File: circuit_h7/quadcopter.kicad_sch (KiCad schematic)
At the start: 110 parts, among them J10 Conn_01x01_Female, J11 Conn_01x04_Male, J12 Conn_01x04_Male, J13 Conn_01x01_Female, J16 Conn_01x01_Female, J17 Conn_01x01_Female, J18 USB_C_Receptacle_USB2.0, J19 Conn_01x08_Male, J21 Conn_01x01_Female, J22 Conn_01x01_Female, J23 Conn_01x01_Female, J24 Conn_01x01_Female, J25 Conn_01x01_Female, J26 Conn_01x01_Female, J28 Conn_01x01_Female, J29 Conn_01x01_Female, J3 Conn_01x01_Female, J30 Conn_01x01_Female, J31 Conn_01x01_Female, J32 Conn_01x01_Female, J33 Conn_01x01_Female, J37 Conn_01x01_Female, J4 Conn_01x01_Female, J40 Conn_01x01_Female, J41 Conn_01x01_Female, J42 Conn_01x01_Female, J43 Conn_01x01_Female, J44 Conn_01x01_Female, J45 Conn_01x01_Female, J47 Conn_01x01_Female, J48 Conn_01x01_Female, J49 Conn_01x01_Female, J5 Conn_Coaxial, J50 Conn_01x01_Female, J6 Conn_01x06_Male, J7 Conn_01x01_Female, J8 Conn_01x01_Female, J9 Conn_01x01_Female, Q1 AO3400A, SW1 SW_DIP_x01, U1 STM32F103VDHx, U2 ICM-42605, U3 DPS310, U4 3V3, U5 EUP3458 1.2A, 30V max input, 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, U6 2450FM07D0034T, U7 W25Q80DVUXIE TR (16M), U8 SX1281, U9 5v, 500mA, Y1 16M, Y2 52Mhz, 12pF

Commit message: Refactored baro/alt module, including applying calibration and temp comp
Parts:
- removed R6: 510, Resistor_SMD:R_0402_1005Metric, symbol Device:R
- added J?: Conn_01x06_Male, Connector_JST:JST_SH_BM06B-SRSS-TB_1x06-1MP_P1.00mm_Vertical, symbol Connector:Conn_01x06_Male
- U7: footprint Anyleaf_Shared:USON-8_2.0x3.0mm_P0.5mm -> Package_SON:WSON-8-1EP_6x5mm_P1.27mm_EP3.4x4.3mm; Digikey W25Q80DVUXIETR-ND -> (none)
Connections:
- net +10V: now also J?.6 (Pin_6)
- net GND: now also J?.2 (Pin_2), J?.5 (Pin_5)
- net UART1_RX: now also J?.1 (Pin_1)
- net UART2_RX: now also J?.3 (Pin_3)
- net UART2_TX: now also J?.4 (Pin_4)
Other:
- note removed: "todo: Bigger flash, on back side?"
- moved on the sheet: J6

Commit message: refactored state into sep module; moved some code to statevolatile that were individual resources.
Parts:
- removed J?: Conn_01x06_Male, Connector_JST:JST_SH_BM06B-SRSS-TB_1x06-1MP_P1.00mm_Vertical, symbol Connector:Conn_01x06_Male
- removed U1: STM32F103VDHx, Package_BGA:LFBGA-100_10x10mm_Layout10x10_P0.8mm, symbol MCU_ST_STM32F1:STM32F103VDHx
- added J1: Conn_01x04_Male, Connector_JST:JST_SH_SM04B-SRSS-TB_1x04-1MP_P1.00mm_Horizontal, symbol Connector:Conn_01x04_Male
- added J14, J2: Conn_01x01_Female, TestPoint:TestPoint_Pad_2.0x2.0mm, symbol Connector:Conn_01x01_Female
- added U1: STM32H723VGH6, Package_BGA:TFBGA-100_8x8mm_Layout10x10_P0.8mm, symbol Anyleaf_Shared:STM32H723VGH6
- J13, J25, J26, J28, J29, J4: footprint TestPoint:TestPoint_Pad_1.5x1.5mm -> TestPoint:TestPoint_Pad_2.0x2.0mm
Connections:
- net +3V3: now also J1.4 (Pin_4), U1.B2 (VBAT), U1.D2 (VDD), U1.F4 (VDD), U1.F5 (VDD), U1.H1 (VDDA), U1.K1 (VDD); no longer U7.3 (IO2), U7.7 (IO3)
- net BATT_DIV: now also U1.C3 (PE4)
- net BOOT0: now also U1.B4 (PB8), U1.D5 (BOOT0)
- net BUZZER_PWM: now also U1.G6 (PE10)
- net CS_ELRS: now also U1.B1 (PC15-OSC32_OUT)
- net CS_FLASH: now also U1.F10 (PC6)
- net CS_IMU: now also U1.K8 (PB12)
- net CUR_DIV: now also U1.G5 (PB2)
- net ELRS_BUSY: now also U1.A1 (PC14-OSC32_IN)
- net ELRS_DIO: now also U1.A2 (PC13)
- net GND: now also J1.3 (Pin_3), U1.C2 (VSS), U1.E4 (VSS), U1.E5 (VSS), U1.E6 (VSS), U1.F7 (PDR_ON), U1.G1 (VSSA), U1.J1 (VSS)
- net IMU_INTERRUPT: now also U1.G4 (PC4)
- net M1: now also U1.D4 (PE0)
- net M2: now also U1.C4 (PE1)
- net M3: now also U1.J4 (PB0)
- net M4: now also U1.K4 (PB1)
- net MISO_1: now also U1.E3 (PE6)
- net MISO_2: now also U1.H10 (PB14)
- net MISO_3: now also U1.A6 (PB4)
- net MOSI_1: now also U1.H5 (PE7)
- net MOSI_2: now also U1.G10 (PB15)
- net MOSI_3: now also U1.C5 (PB5)
- net NRST: now also U1.E1 (NRST)
- net OSC_IN: now also U1.C1 (PH0-OSC_IN)
- net OSC_OUT: now also U1.D1 (PH1-OSC_OUT)
- net SCK_1: now also U1.D3 (PE5)
- net SCK_2: now also U1.J8 (PB13)
- net SCK_3: now also U1.A7 (PB3)
- net SCL1: now also J1.1 (Pin_1), U1.H7 (PE15)
- net SCL2: now also U1.K5 (PE9)
- net SDA1: now also J1.2 (Pin_2), U1.A4 (PB9)
- net SDA2: now also U1.J5 (PE8)
- net SWCLK: now also U1.G7 (PE14)
- net SWDIO: now also U1.K6 (PE13)
- net UART1_RX: now also U1.A5 (PB7)
- net UART1_TX: now also U1.B5 (PB6)
- net UART2_RX: now also U1.B3 (PE3)
- net UART2_TX: now also U1.A3 (PE2)
- net UART3_RX: now also U1.K7 (PB11)
- net UART3_TX: now also U1.J7 (PB10)
- net UART4_RX: now also U1.B8 (PC11)
- net UART4_TX: now also U1.C8 (PC12)
- net USB_DN: now also U1.H6 (PE11)
- net USB_DP: now also U1.J6 (PE12)
- new net QSPI2_IO2: U7.3 (IO2)
- new net QSPI2_IO3: U7.7 (IO3)
- new net UART5_RX: J14.1 (Pin_1)
- new net UART5_TX: J2.1 (Pin_1)
- no-connect marks 8 -> 11
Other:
- moved on the sheet: C10, C11, C12, C13, C16, C17, C18, C6, C9, J11, J12, J40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

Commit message: More work on routing
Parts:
- added J15: Conn_01x01_Female, TestPoint:TestPoint_Pad_2.0x2.0mm, symbol Connector:Conn_01x01_Female
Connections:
- net +3V3: now also J15.1 (Pin_1)
- net BATT_DIV: now also U1.G3 (PA4); no longer U1.C3 (PE4)
- net BUZZER_PWM: now also U1.D10 (PA10); no longer U1.G6 (PE10)
- net CS_FLASH: now also U1.B9 (PC10); no longer U1.F10 (PC6)
- net CS_IMU: now also U1.G4 (PC4); no longer U1.K8 (PB12)
- net IMU_INTERRUPT: now also U1.K8 (PB12); no longer U1.G4 (PC4)
- net M1: now also U1.F10 (PC6); no longer U1.D4 (PE0)
- net M2: now also U1.E10 (PC7); no longer U1.C4 (PE1)
- net M3: now also U1.F9 (PC8); no longer U1.J4 (PB0)
- net M4: now also U1.E9 (PC9); no longer U1.K4 (PB1)
- net MISO_1: now also U1.J3 (PA6); no longer U1.E3 (PE6)
- net MOSI_1: now also U1.K3 (PA7); no longer U1.H5 (PE7)
- net SCK_1: now also U1.H3 (PA5); no longer U1.D3 (PE5)
- net SCL1: now also U1.A8 (PA15); no longer U1.H7 (PE15)
- net SCL2: now also U1.C9 (PA9); no longer U1.K5 (PE9)
- net SDA2: now also U1.D9 (PA8); no longer U1.J5 (PE8)
- net SWCLK: now also U1.A9 (PA14); no longer U1.G7 (PE14)
- net SWDIO: now also U1.A10 (PA13); no longer U1.K6 (PE13)
- net UART2_RX: now also U1.K2 (PA3); no longer U1.B3 (PE3)
- net UART2_TX: now also U1.J2 (PA2); no longer U1.A3 (PE2)
- net USB_DN: now also U1.C10 (PA11); no longer U1.H6 (PE11)
- net USB_DP: now also U1.B10 (PA12); no longer U1.J6 (PE12)
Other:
- moved on the sheet: J17, J33

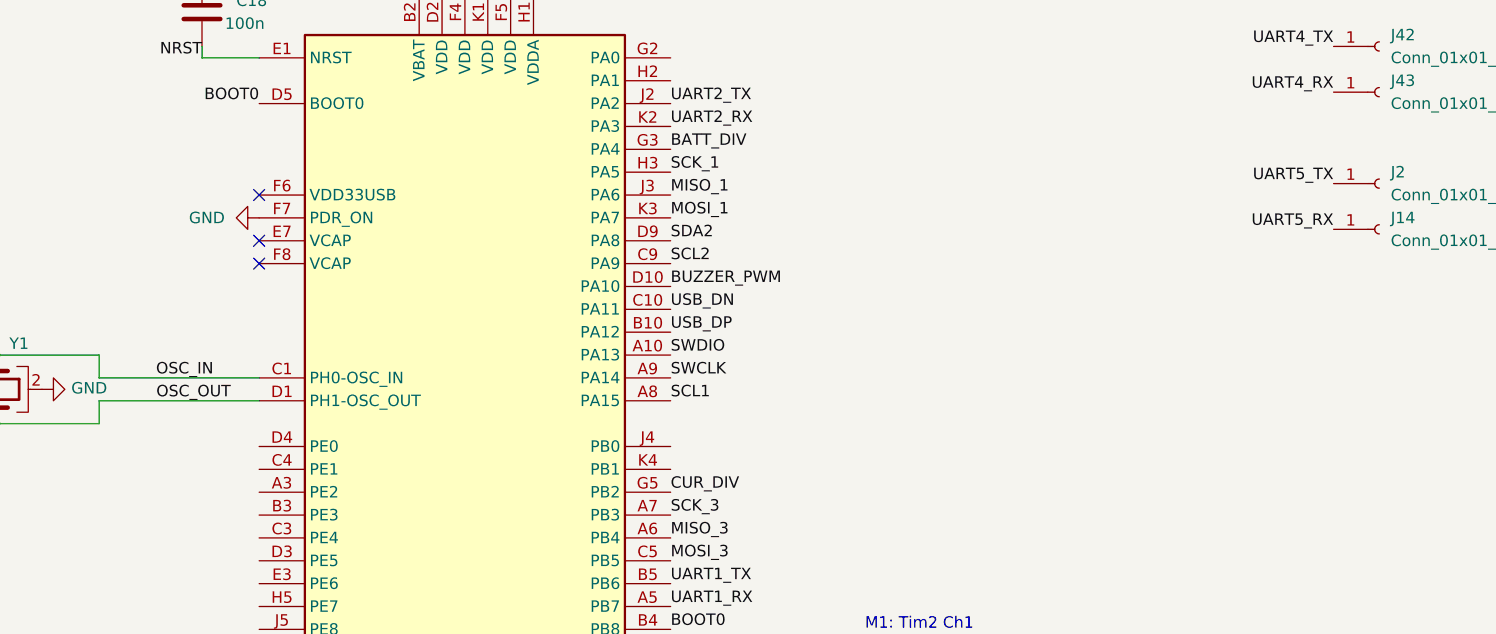
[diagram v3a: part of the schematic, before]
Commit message: Started switch to PID setup where starting point is prev control settings; no 0
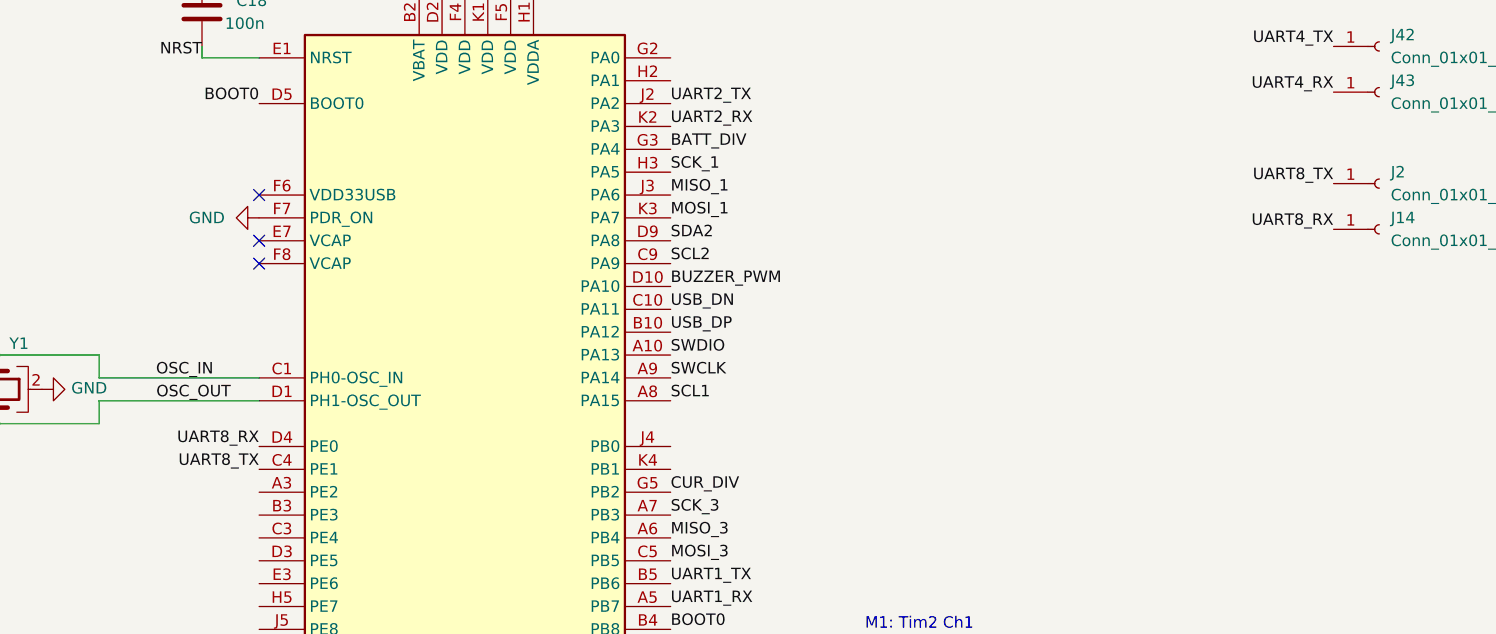
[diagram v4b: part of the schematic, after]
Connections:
- net UART5_RX is gone; now on net UART8_RX: J14.1 (Pin_1)
- net UART5_TX is gone; now on net UART8_TX: J2.1 (Pin_1)
- net UART8_TX: now reaches U1.C4 (PE1)
- net UART8_RX: now reaches U1.D4 (PE0)
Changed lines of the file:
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@@
     (effects (font (size 1.27 1.27)) (justify left bottom))
   )
-  (label "UART5_TX" (at 381 257.81 180)
+  (label "UART8_TX" (at 381 257.81 180)
     (effects (font (size 1.27 1.27)) (justify right bottom))
   )
@@
     (effects (font (size 1.27 1.27)) (justify left bottom))
   )
+  (label "UART8_TX" (at 261.62 289.56 180)
+    (effects (font (size 1.27 1.27)) (justify right bottom))
+  )
   (label "UART3_RX" (at 307.34 314.96 0)
     (effects (font (size 1.27 1.27)) (justify left bottom))
@@
   )
   (label "UART2_TX" (at 440.69 102.87 180)
+    (effects (font (size 1.27 1.27)) (justify right bottom))
+  )
+  (label "UART8_RX" (at 261.62 287.02 180)
     (effects (font (size 1.27 1.27)) (justify right bottom))
   )
@@
     (effects (font (size 1.27 1.27)) (justify right bottom))
   )
-  (label "UART5_RX" (at 381 262.89 180)
+  (label "UART8_RX" (at 381 262.89 180)
     (effects (font (size 1.27 1.27)) (justify right bottom))
   )

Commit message: added tx pwr enum, and pass to preflight
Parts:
- J6: footprint Connector_JST:JST_SH_BM06B-SRSS-TB_1x06-1MP_P1.00mm_Vertical -> Connector_JST:JST_GH_SM06B-GHS-TB_1x06-1MP_P1.25mm_Horizontal
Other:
- note removed: "Consider Johanson 2450FM07D0034T: It's a 0402 IC specicially designed to filter this chip."
- note removed: "todo: Change resistor value to dim LED!!!"
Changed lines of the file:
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@@
     (effects (font (size 1.27 1.27)) (justify left bottom))
   )
-  (text "Consider Johanson 2450FM07D0034T: It's a \n0402 IC specicially designed to filter this chip."
-    (at 95.25 294.64 0)
-    (effects (font (size 1.27 1.27)) (justify left bottom))
-  )
   (text "5v on USART lines?\n" (at 80.01 152.4 0)
     (effects (font (size 1.27 1.27)) (justify left bottom))
@@
     (effects (font (size 1.27 1.27)) (justify left bottom))
   )
-  (text "todo: Change resistor value to dim LED!!!" (at 209.55 71.12 0)
-    (effects (font (size 1.27 1.27)) (justify left bottom))
-  )
   (text "Ground pins 2 and 3 for ISM330 compatibility.\nDoesn't matter for ICM42605\n"
     (at 189.23 154.94 0)
@@
       (effects (font (size 1.27 1.27)) (justify right))
     )
-    (property "Footprint" "Connector_JST:JST_SH_BM06B-SRSS-TB_1x06-1MP_P1.00mm_Vertical" (id 2) (at 509.27 106.68 0)
+    (property "Footprint" "Connector_JST:JST_GH_SM06B-GHS-TB_1x06-1MP_P1.25mm_Horizontal" (id 2) (at 509.27 106.68 0)
       (effects (font (size 1.27 1.27)) hide)
     )
@@
     )
     (path "/d6b17d43-2233-4afb-a36d-bd05ee59e3bb"
-      (reference "J6") (unit 1) (value "Conn_01x06_Male") (footprint "Connector_JST:JST_SH_BM06B-SRSS-TB_1x06-1MP_P1.00mm_Vertical")
+      (reference "J6") (unit 1) (value "Conn_01x06_Male") (footprint "Connector_JST:JST_GH_SM06B-GHS-TB_1x06-1MP_P1.25mm_Horizontal")
     )
     (path "/e491e9c4-83e3-4bb2-8ba8-b05d76f48b2c"

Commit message: Added code to store waypoints with names
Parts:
- added C?: 10u, Capacitor_SMD:C_0402_1005Metric, symbol Device:C
- added C?: 6.8p, Capacitor_SMD:C_0402_1005Metric, symbol Device:C
- added C?: 100n, Capacitor_SMD:C_0402_1005Metric, symbol Device:C
- added C?: 1u 50V, Capacitor_SMD:C_0603_1608Metric, symbol Device:C
- added C?: 12p, Capacitor_SMD:C_0402_1005Metric, symbol Device:C
- added R?: 10k, Resistor_SMD:R_0402_1005Metric, symbol Device:R
- added U10: ESP8285, Package_DFN_QFN:QFN-32-1EP_5x5mm_P0.5mm_EP3.45x3.45mm, symbol MCU_Espressif:ESP8266EX
- added U11: ESP32-PICO-D4, Package_DFN_QFN:QFN-48-1EP_7x7mm_P0.5mm_EP5.3x5.3mm, symbol RF_Module:ESP32-PICO-D4
- added Y?: 16M, Crystal:Crystal_SMD_2016-4Pin_2.0x1.6mm, symbol Device:Crystal_GND24
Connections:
- net +3V3: now also C?.2, C?.2, R?.2, U10.1 (VDDA), U10.11 (VDDPST), U10.17 (VDDPST), U10.29 (VDDD), U10.3 (VDD3P3), U10.30 (VDDA), U10.4 (VDD3P3), U10.5 (VDD_RTC)
- net GND: now also C?.1, C?.1, C?.1, C?.1, C?.1, U10.33 (GND), Y?.2, Y?.4
- new net: U11.1 (VDDA), U11.43 (VDDA), U11.46 (VDDA)
- new net: U11.3 (VDDA3P3), U11.4 (VDDA3P3)
- new net: C?.2, Y?.1
- new net: C?.2, Y?.3
- new net: C?.2, R?.1

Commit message: H7 fixes
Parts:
- removed C?: 1u 50V, Capacitor_SMD:C_0603_1608Metric, symbol Device:C
- removed J1: Conn_01x04_Male, Connector_JST:JST_SH_SM04B-SRSS-TB_1x04-1MP_P1.00mm_Horizontal, symbol Connector:Conn_01x04_Male
- removed U11: ESP32-PICO-D4, Package_DFN_QFN:QFN-48-1EP_7x7mm_P0.5mm_EP5.3x5.3mm, symbol RF_Module:ESP32-PICO-D4
- added C34, C37: 1u 25v, Capacitor_SMD:C_0402_1005Metric, symbol Device:C
- added D6: LED, LED_SMD:LED_0603_1608Metric, symbol Device:LED
- added J1, J20: Conn_01x01_Female, TestPoint:TestPoint_Pad_1.0x1.0mm, symbol Connector:Conn_01x01_Female
- added R9: 3.3k, Resistor_SMD:R_0402_1005Metric, symbol Device:R
- J11: footprint Connector_JST:JST_SH_SM04B-SRSS-TB_1x04-1MP_P1.00mm_Horizontal -> Connector_JST:JST_GH_SM04B-GHS-TB_1x04-1MP_P1.25mm_Horizontal; LCSC (none) -> C189895
- J19: footprint Connector_JST:JST_SH_SM08B-SRSS-TB_1x08-1MP_P1.00mm_Horizontal -> Connector_JST:JST_GH_SM08B-GHS-TB_1x08-1MP_P1.25mm_Horizontal; LCSC C160407 -> C265111
- Y3: renamed from Y?; value 16M -> 40M
- gave numbers to parts that had none: 5
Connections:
- net +3V3: now also C37.1
- net CS_ELRS: now also U10.13 (MTDO), U10.32 (~{EXT_RSTB}); no longer U1.B1 (PC15-OSC32_OUT)
- net ELRS_BUSY: now also U10.24 (GPIO5); no longer U1.A1 (PC14-OSC32_IN)
- net ELRS_DIO: now also U10.16 (GPIO4); no longer U1.A2 (PC13)
- net ELRS_RST: now also U10.14 (GPIO2)
- net GND: now also C34.2, C37.2, D6.1 (K)
- net MISO_3: no longer U1.A6 (PB4), U8.16 (MISO_TX)
- net MISO_ELRS: now also U10.10 (MTDI), U8.16 (MISO_TX)
- net MOSI_3: no longer U1.C5 (PB5), U8.17 (MOSI_RX)
- net MOSI_ELRS: now also U10.12 (MTCK), U8.17 (MOSI_RX)
- net SCK_3: no longer U1.A7 (PB3), U8.18 (SCK_RTSN)
- net SCK_ELRS: now also U10.9 (MTMS), U8.18 (SCK_RTSN)
- net ANT_TRACE: now reaches U10.2 (LNA)
- net RX_ELRS: now reaches U10.25 (U0RXD)
- net RX_ELRS: now also J20.1 (Pin_1)
- net TX_ELRS: now reaches U10.26 (U0TXD)
- net TX_ELRS: now also J1.1 (Pin_1)
- net at U10.27 (XTAL_OUT): now also C32.2, Y3.1
- net at U10.28 (XTAL_IN): now also C33.2, Y3.3
- net at U10.7 (CHIP_PU): now also R6.1, C34.1
- net at U10.8 (XPD_DCDC): now also R9.2
- new net: D6.2 (A), R9.1
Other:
- note added: "24-52Mhz crystal"
- note added: "Pads for flashing the ELRS MCU"
- note added: "Todo: second I2C GH port?"
- note added: "Undocumented guideline for pinout: https://github.com/ExpressLRS/ExpressLRS/blob/master/src/hardware/RX/Generic%202400.json"
